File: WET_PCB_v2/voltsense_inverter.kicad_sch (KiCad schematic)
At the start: 9 parts, among them J17 Capacitor connector, J19 Capacitor connector, U3 Opamp_Quad

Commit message: notees
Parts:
- removed D7, D8: 1N4004, Diode_THT:D_DO-15_P2.54mm_Vertical_CathodeUp, symbol Diode:1N4004
- added D31, D32: D_Zener, Diode_THT:D_DO-15_P2.54mm_Vertical_CathodeUp, symbol Device:D_Zener
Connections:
- net GND: now also D32.2 (A)
- net VDD_OPAMP: now also D31.1 (K)
- net Vsense_ADC: now also D31.2 (A), D32.1 (K)
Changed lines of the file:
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@@
-	)
-	(symbol
-		(lib_id "Diode:1N4004")
-		(at 128.27 45.72 90)
-		(mirror x)
-		(unit 1)
-		(body_style 1)
-		(exclude_from_sim no)
-		(in_bom yes)
-		(on_board yes)
-		(in_pos_files yes)
-		(dnp no)
-		(fields_autoplaced yes)
-		(property "Reference" "D7"
-			(at 130.81 44.4499 90)
-			(show_name no)
-			(do_not_autoplace no)
-			(effects
-				(font
-					(size 1.27 1.27)
-				)
-				(justify right)
-			)
-		)
-		(property "Value" "1N4004"
-			(at 130.81 46.9899 90)
-			(show_name no)
-			(do_not_autoplace no)
-			(effects
-				(font
-					(size 1.27 1.27)
-				)
-				(justify right)
-			)
-		)
-		(property "Footprint" "Diode_THT:D_DO-15_P2.54mm_Vertical_CathodeUp"
-			(at 132.715 45.72 0)
-			(hide yes)
-			(show_name no)
-			(do_not_autoplace no)
-			(effects
-				(font
-					(size 1.27 1.27)
-				)
-			)
-		)
-		(property "Datasheet" "http://www.vishay.com/docs/88503/1n4001.pdf"
-			(at 128.27 45.72 0)
-			(hide yes)
-			(show_name no)
-			(do_not_autoplace no)
-			(effects
-				(font
-					(size 1.27 1.27)
-				)
-			)
-		)
-		(property "Description" "400V 1A General Purpose Rectifier Diode, DO-41"
-			(at 128.27 45.72 0)
-			(hide yes)
-			(show_name no)
-			(do_not_autoplace no)
-			(effects
-				(font
-					(size 1.27 1.27)
-				)
-			)
-		)
-		(property "Sim.Device" "D"
-			(at 128.27 45.72 0)
-			(hide yes)
-			(show_name no)
-			(do_not_autoplace no)
-			(effects
-				(font
-					(size 1.27 1.27)
-				)
-			)
-		)
-		(property "Sim.Pins" "1=K 2=A"
-			(at 128.27 45.72 0)
-			(hide yes)
-			(show_name no)
-			(do_not_autoplace no)
-			(effects
-				(font
-					(size 1.27 1.27)
-				)
-			)
-		)
-		(pin "1"
-		)
-		(pin "2"
-		)
-		(instances
-			(project "WET_PCB_v2"
-				(path "/13451c35-1666-47d9-9525-8d8125ba1cf3/419c9796-b7e1-43c1-b033-dc2479750a67"
-					(reference "D7")
-					(unit 1)
-				)
-			)
-		)
 	)
 	(symbol
@@
 	)
 	(symbol
+		(lib_id "Device:D_Zener")
+		(at 128.27 45.72 270)
+		(unit 1)
+		(body_style 1)
+		(exclude_from_sim no)
+		(in_bom yes)
+		(on_board yes)
+		(in_pos_files yes)
+		(dnp no)
+		(fields_autoplaced yes)
+		(property "Reference" "D31"
+			(at 130.81 44.4499 90)
+			(show_name no)
+			(do_not_autoplace no)
+			(effects
+				(font
+					(size 1.27 1.27)
+				)
+				(justify left)
+			)
+		)
+		(property "Value" "D_Zener"
+			(at 130.81 46.9899 90)
+			(show_name no)
+			(do_not_autoplace no)
+			(effects
+				(font
+					(size 1.27 1.27)
+				)
+				(justify left)
+			)
+		)
+		(property "Footprint" "Diode_THT:D_DO-15_P2.54mm_Vertical_CathodeUp"
+			(at 128.27 45.72 0)
+			(hide yes)
+			(show_name no)
+			(do_not_autoplace no)
+			(effects
+				(font
+					(size 1.27 1.27)
+				)
+			)
+		)
+		(property "Datasheet" ""
+			(at 128.27 45.72 0)
+			(hide yes)
+			(show_name no)
+			(do_not_autoplace no)
+			(effects
+				(font
+					(size 1.27 1.27)
+				)
+			)
+		)
+		(property "Description" "Zener diode"
+			(at 128.27 45.72 0)
+			(hide yes)
+			(show_name no)
+			(do_not_autoplace no)
+			(effects
+				(font
+					(size 1.27 1.27)
+				)
+			)
+		)
+		(pin "2"
+		)
+		(pin "1"
+		)
+		(instances
+			(project "WET_PCB_v2"
+				(path "/13451c35-1666-47d9-9525-8d8125ba1cf3/419c9796-b7e1-43c1-b033-dc2479750a67"
+					(reference "D31")
+					(unit 1)
+				)
+			)
+		)
+	)
+	(symbol
 		(lib_id "Connector_Generic:Conn_02x01")
 		(at 62.23 59.69 90)
@@
 	)
 	(symbol
+		(lib_id "Device:D_Zener")
+		(at 128.27 55.88 270)
+		(unit 1)
+		(body_style 1)
+		(exclude_from_sim no)
+		(in_bom yes)
+		(on_board yes)
+		(in_pos_files yes)
+		(dnp no)
+		(fields_autoplaced yes)
+		(property "Reference" "D32"
+			(at 130.81 54.6099 90)
+			(show_name no)
+			(do_not_autoplace no)
+			(effects
+				(font
+					(size 1.27 1.27)
+				)
+				(justify left)
+			)
+		)
+		(property "Value" "D_Zener"
+			(at 130.81 57.1499 90)
+			(show_name no)
+			(do_not_autoplace no)
+			(effects
+				(font
+					(size 1.27 1.27)
+				)
+				(justify left)
+			)
+		)
+		(property "Footprint" "Diode_THT:D_DO-15_P2.54mm_Vertical_CathodeUp"
+			(at 128.27 55.88 0)
+			(hide yes)
+			(show_name no)
+			(do_not_autoplace no)
+			(effects
+				(font
+					(size 1.27 1.27)
+				)
+			)
+		)
+		(property "Datasheet" ""
+			(at 128.27 55.88 0)
+			(hide yes)
+			(show_name no)
+			(do_not_autoplace no)
+			(effects
+				(font
+					(size 1.27 1.27)
+				)
+			)
+		)
+		(property "Description" "Zener diode"
+			(at 128.27 55.88 0)
+			(hide yes)
+			(show_name no)
+			(do_not_autoplace no)
+			(effects
+				(font
+					(size 1.27 1.27)
+				)
+			)
+		)
+		(pin "2"
+		)
+		(pin "1"
+		)
+		(instances
+			(project "WET_PCB_v2"
+				(path "/13451c35-1666-47d9-9525-8d8125ba1cf3/419c9796-b7e1-43c1-b033-dc2479750a67"
+					(reference "D32")
+					(unit 1)
+				)
+			)
+		)
+	)
+	(symbol
 		(lib_id "power:GND")
 		(at 128.27 59.69 0)
@@
 					(unit 1)
 				)
-			)
-		)
-	)
-	(symbol
-		(lib_id "Diode:1N4004")
-		(at 128.27 55.88 90)
-		(mirror x)
-		(unit 1)
-		(body_style 1)
-		(exclude_from_sim no)
-		(in_bom yes)
-		(on_board yes)
-		(in_pos_files yes)
-		(dnp no)
-		(fields_autoplaced yes)
-		(property "Reference" "D8"
-			(at 130.81 54.6099 90)
-			(show_name no)
-			(do_not_autoplace no)
-			(effects
-				(font
-					(size 1.27 1.27)
-				)
-				(justify right)
-			)
-		)
-		(property "Value" "1N4004"
-			(at 130.81 57.1499 90)
-			(show_name no)
-			(do_not_autoplace no)
-			(effects
-				(font
-					(size 1.27 1.27)
-				)
-				(justify right)
-			)
-		)
-		(property "Footprint" "Diode_THT:D_DO-15_P2.54mm_Vertical_CathodeUp"
-			(at 132.715 55.88 0)
-			(hide yes)
-			(show_name no)
-			(do_not_autoplace no)
-			(effects
-				(font
-					(size 1.27 1.27)
-				)
-			)
-		)
-		(property "Datasheet" "http://www.vishay.com/docs/88503/1n4001.pdf"
-			(at 128.27 55.88 0)
-			(hide yes)
-			(show_name no)
-			(do_not_autoplace no)
-			(effects
-				(font
-					(size 1.27 1.27)
-				)
-			)
-		)
-		(property "Description" "400V 1A General Purpose Rectifier Diode, DO-41"
-			(at 128.27 55.88 0)
-			(hide yes)
-			(show_name no)
-			(do_not_autoplace no)
-			(effects
-				(font
-					(size 1.27 1.27)
-				)
-			)
-		)
-		(property "Sim.Device" "D"
-			(at 128.27 55.88 0)
-			(hide yes)
-			(show_name no)
-			(do_not_autoplace no)
-			(effects
-				(font
-					(size 1.27 1.27)
-				)
-			)
-		)
-		(property "Sim.Pins" "1=K 2=A"
-			(at 128.27 55.88 0)
-			(hide yes)
-			(show_name no)
-			(do_not_autoplace no)
-			(effects
-				(font
-					(size 1.27 1.27)
-				)
-			)
-		)
-		(pin "1"
-		)
-		(pin "2"
-		)
-		(instances
-			(project "WET_PCB_v2"
-				(path "/13451c35-1666-47d9-9525-8d8125ba1cf3/419c9796-b7e1-43c1-b033-dc2479750a67"
-					(reference "D8")
-					(unit 1)
-				)

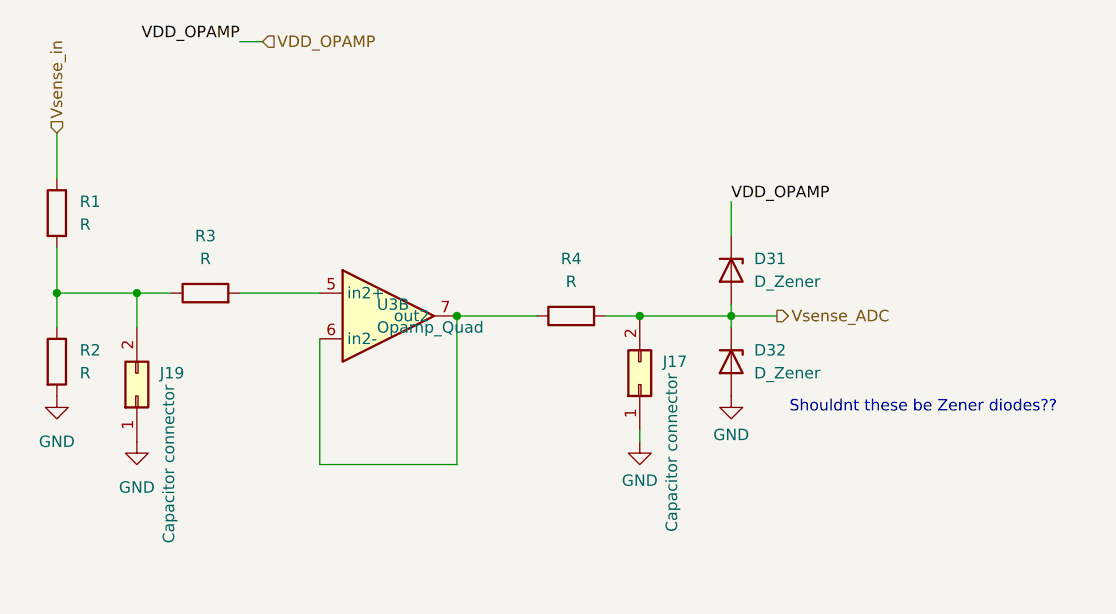
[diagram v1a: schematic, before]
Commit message: redid part of layout inverter
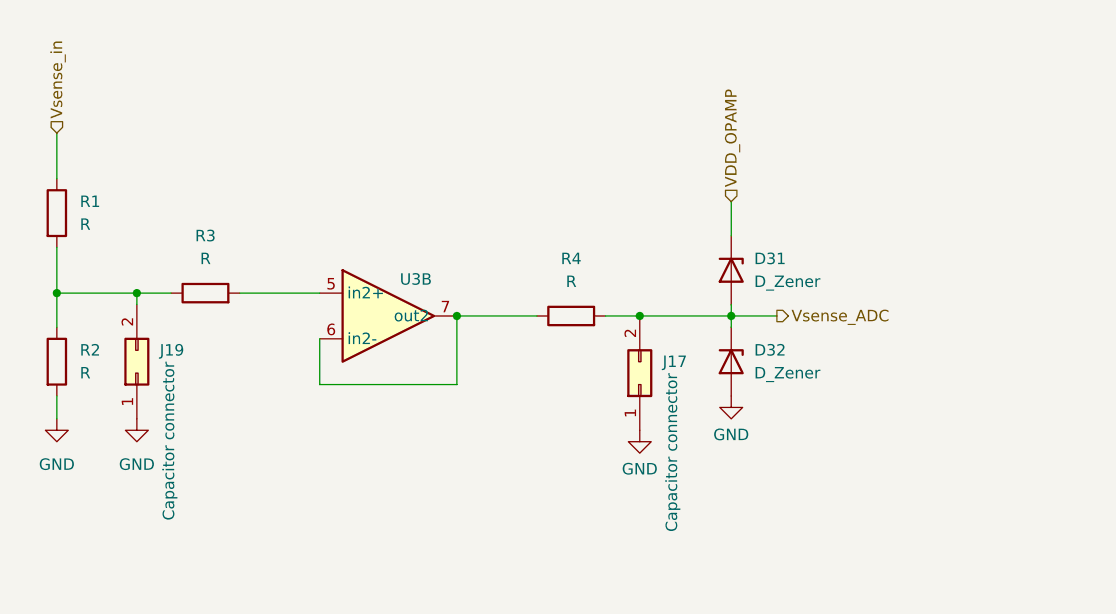
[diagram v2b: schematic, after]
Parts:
- R1, R2, R3, R4: footprint Resistor_THT:R_Axial_DIN0207_L6.3mm_D2.5mm_P7.62mm_Horizontal -> Resistor_SMD:R_0805_2012Metric_Pad1.20x1.40mm_HandSolder
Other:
- note removed: "Shouldnt these be Zener diodes??"
- moved on the sheet: J19
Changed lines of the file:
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@@
 	(generator_version "10.0")
 	(paper "A4")
-	(text "Shouldnt these be Zener diodes??\n"
-		(exclude_from_sim no)
-		(at 149.606 60.96 0)
-		(effects
-			(font
-				(size 1.27 1.27)
-			)
-		)
-	)
 	(junction
 		(at 53.34 48.26)
@@
 	)
 	(junction
+		(at 62.23 48.26)
+		(diameter 0)
+		(color 0 0 0 0)
+	)
+	(junction
 		(at 128.27 50.8)
 		(diameter 0)
@@
 	)
 	(junction
-		(at 62.23 48.26)
+		(at 118.11 50.8)
 		(diameter 0)
 		(color 0 0 0 0)
@@
 		(color 0 0 0 0)
 	)
-	(junction
-		(at 118.11 50.8)
-		(diameter 0)
-		(color 0 0 0 0)
-	)
-	(wire
-		(pts
-			(xy 62.23 48.26) (xy 62.23 52.07)
-		)
-		(stroke
-			(width 0)
-			(type default)
-		)
-	)
 	(wire
 		(pts
@@
 	(wire
 		(pts
-			(xy 82.55 53.34) (xy 82.55 67.31)
+			(xy 82.55 53.34) (xy 82.55 58.42)
 		)
 		(stroke
@@
 	(wire
 		(pts
+			(xy 62.23 49.53) (xy 62.23 48.26)
+		)
+		(stroke
+			(width 0)
+			(type default)
+		)
+	)
+	(wire
+		(pts
 			(xy 114.3 50.8) (xy 118.11 50.8)
 		)
@@
 	(wire
 		(pts
-			(xy 118.11 63.5) (xy 118.11 64.77)
-		)
-		(stroke
-			(width 0)
-			(type default)
-		)
-	)
-	(wire
-		(pts
 			(xy 53.34 48.26) (xy 53.34 52.07)
 		)
@@
 	(wire
 		(pts
-			(xy 97.79 50.8) (xy 97.79 67.31)
+			(xy 97.79 50.8) (xy 97.79 58.42)
+		)
+		(stroke
+			(width 0)
+			(type default)
+		)
+	)
+	(wire
+		(pts
+			(xy 53.34 62.23) (xy 53.34 59.69)
 		)
 		(stroke
@@
 	(wire
 		(pts
-			(xy 76.2 20.32) (xy 73.66 20.32)
-		)
-		(stroke
-			(width 0)
-			(type default)
-		)
-	)
-	(wire
-		(pts
 			(xy 62.23 48.26) (xy 66.04 48.26)
 		)
@@
 	(wire
 		(pts
-			(xy 82.55 67.31) (xy 97.79 67.31)
-		)
-		(stroke
-			(width 0)
-			(type default)
-		)
-	)
-	(label "VDD_OPAMP"
-		(at 128.27 38.1 0)
-		(effects
-			(font
-				(size 1.27 1.27)
-			)
-			(justify left bottom)
-		)
-	)
-	(label "VDD_OPAMP"
-		(at 73.66 20.32 180)
-		(effects
-			(font
-				(size 1.27 1.27)
-			)
-			(justify right bottom)
-		)
-	)
-	(hierarchical_label "VDD_OPAMP"
-		(shape input)
-		(at 76.2 20.32 0)
-		(effects
-			(font
-				(size 1.27 1.27)
-			)
-			(justify left)
+			(xy 82.55 58.42) (xy 97.79 58.42)
+		)
+		(stroke
+			(width 0)
+			(type default)
 		)
 	)
@@
 		(shape input)
 		(at 53.34 30.48 90)
+		(effects
+			(font
+				(size 1.27 1.27)
+			)
+			(justify left)
+		)
+	)
+	(hierarchical_label "VDD_OPAMP"
+		(shape input)
+		(at 128.27 38.1 90)
 		(effects
 			(font
@@
 			)
 		)
-		(property "Footprint" "Resistor_THT:R_Axial_DIN0207_L6.3mm_D2.5mm_P7.62mm_Horizontal"
+		(property "Footprint" "Resistor_SMD:R_0805_2012Metric_Pad1.20x1.40mm_HandSolder"
 			(at 110.49 52.578 90)
 			(hide yes)
@@
 			)
 		)
-		(property "Footprint" "Resistor_THT:R_Axial_DIN0207_L6.3mm_D2.5mm_P7.62mm_Horizontal"
+		(property "Footprint" "Resistor_SMD:R_0805_2012Metric_Pad1.20x1.40mm_HandSolder"
 			(at 51.562 55.88 90)
 			(hide yes)
@@
 	(symbol
 		(lib_id "Connector_Generic:Conn_02x01")
-		(at 62.23 59.69 90)
+		(at 62.23 57.15 90)
 		(unit 1)
 		(body_style 1)
@@
 		(dnp no)
 		(property "Reference" "J19"
-			(at 64.77 57.1499 90)
+			(at 64.77 54.6099 90)
 			(show_name no)
 			(do_not_autoplace no)
@@
 		)
 		(property "Value" "Capacitor connector"
-			(at 65.786 58.42 0)
+			(at 65.786 55.88 0)
 			(show_name no)
 			(do_not_autoplace no)
@@
 		)
 		(property "Footprint" "Connector_PinSocket_2.54mm:PinSocket_1x02_P2.54mm_Vertical"
-			(at 62.23 59.69 0)
+			(at 62.23 57.15 0)
 			(hide yes)
 			(show_name no)
@@
 		)
 		(property "Datasheet" ""
-			(at 62.23 59.69 0)
+			(at 62.23 57.15 0)
 			(hide yes)
 			(show_name no)
@@
 		)
 		(property "Description" "Generic connector, double row, 02x01, this symbol is compatible with counter-clockwise, top-bottom and odd-even numbering schemes., script generated (kicad-library-utils/schlib/autogen/connector/)"
-			(at 62.23 59.69 0)
+			(at 62.23 57.15 0)
 			(hide yes)
 			(show_name no)
@@
 	(symbol
 		(lib_id "power:GND")
-		(at 62.23 64.77 0)
+		(at 62.23 62.23 0)
 		(unit 1)
 		(body_style 1)
@@
 		(fields_autoplaced yes)
 		(property "Reference" "#PWR018"
-			(at 62.23 71.12 0)
+			(at 62.23 68.58 0)
 			(hide yes)
 			(show_name no)
@@
 		)
 		(property "Value" "GND"
-			(at 62.23 69.85 0)
+			(at 62.23 67.31 0)
 			(show_name no)
 			(do_not_autoplace no)
@@
 		)
 		(property "Footprint" ""
-			(at 62.23 64.77 0)
+			(at 62.23 62.23 0)
 			(hide yes)
 			(show_name no)
@@
 		)
 		(property "Datasheet" ""
-			(at 62.23 64.77 0)
+			(at 62.23 62.23 0)
 			(hide yes)
 			(show_name no)
@@
 		)
 		(property "Description" "Power symbol creates a global label with name \"GND\" , ground"
-			(at 62.23 64.77 0)
+			(at 62.23 62.23 0)
 			(hide yes)
 			(show_name no)
@@
 			)
 		)
-		(property "Footprint" "Resistor_THT:R_Axial_DIN0207_L6.3mm_D2.5mm_P7.62mm_Horizontal"
+		(property "Footprint" "Resistor_SMD:R_0805_2012Metric_Pad1.20x1.40mm_HandSolder"
 			(at 69.85 50.038 90)
 			(hide yes)
@@
 		(in_pos_files yes)
 		(dnp no)
-		(fields_autoplaced yes)
 		(property "Reference" "U3"
-			(at 88.9 49.5299 0)
+			(at 91.44 46.736 0)
 			(show_name no)
 			(do_not_autoplace no)
@@
 		)
 		(property "Value" "Opamp_Quad"
-			(at 88.9 52.0699 0)
+			(at 84.836 57.15 0)
+			(hide yes)
 			(show_name no)
 			(do_not_autoplace no)
@@
 	(symbol
 		(lib_id "power:GND")
-		(at 118.11 64.77 0)
+		(at 118.11 63.5 0)
 		(unit 1)
 		(body_style 1)
@@
 		(dnp no)
 		(property "Reference" "#PWR021"
-			(at 118.11 71.12 0)
+			(at 118.11 69.85 0)
 			(hide yes)
 			(show_name no)
@@
 		)
 		(property "Value" "GND"
-			(at 118.11 69.088 0)
+			(at 118.11 67.818 0)
 			(show_name no)
 			(do_not_autoplace no)
@@
 		)
 		(property "Footprint" ""
-			(at 118.11 64.77 0)
+			(at 118.11 63.5 0)
 			(hide yes)
 			(show_name no)
@@
 		)
 		(property "Datasheet" ""
-			(at 118.11 64.77 0)
+			(at 118.11 63.5 0)
 			(hide yes)
 			(show_name no)
@@
 		)
 		(property "Description" "Power symbol creates a global label with name \"GND\" , ground"
-			(at 118.11 64.77 0)
+			(at 118.11 63.5 0)
 			(hide yes)
 			(show_name no)
@@
 			)
 		)
-		(property "Footprint" "Resistor_THT:R_Axial_DIN0207_L6.3mm_D2.5mm_P7.62mm_Horizontal"
+		(property "Footprint" "Resistor_SMD:R_0805_2012Metric_Pad1.20x1.40mm_HandSolder"
 			(at 51.562 39.37 90)
 			(hide yes)
@@
 	(symbol
 		(lib_id "power:GND")
-		(at 53.34 59.69 0)
+		(at 53.34 62.23 0)
 		(unit 1)
 		(body_style 1)
@@
 		(fields_autoplaced yes)
 		(property "Reference" "#PWR017"
-			(at 53.34 66.04 0)
+			(at 53.34 68.58 0)
 			(hide yes)
 			(show_name no)
@@
 		)
 		(property "Value" "GND"
-			(at 53.34 64.77 0)
+			(at 53.34 67.31 0)
 			(show_name no)
 			(do_not_autoplace no)
@@
 		)
 		(property "Footprint" ""
-			(at 53.34 59.69 0)
+			(at 53.34 62.23 0)
 			(hide yes)
 			(show_name no)
@@
 		)
 		(property "Datasheet" ""
-			(at 53.34 59.69 0)
+			(at 53.34 62.23 0)
 			(hide yes)
 			(show_name no)
@@
 		)
 		(property "Description" "Power symbol creates a global label with name \"GND\" , ground"
-			(at 53.34 59.69 0)
-			(hide yes)
-			(show_name no)
+			(at 53.34 62.23 0)
+			(hide yes)
+			(show_name no)

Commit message: didnt watch the lecture but made progress ig
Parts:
- added R41: R0, Resistor_SMD:R_0805_2012Metric_Pad1.20x1.40mm_HandSolder, symbol Device:R
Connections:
- net at R4.1, U3.7 (out2): now also R41.2; no longer U3.6 (in2-)
- new net: R41.1, U3.6 (in2-)
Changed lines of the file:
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@@
+	)
+	(junction
+		(at 100.33 50.8)
+		(diameter 0)
+		(color 0 0 0 0)
 	)
 	(junction
@@
 		(color 0 0 0 0)
 	)
-	(junction
-		(at 97.79 50.8)
-		(diameter 0)
-		(color 0 0 0 0)
+	(wire
+		(pts
+			(xy 95.25 58.42) (xy 100.33 58.42)
+		)
+		(stroke
+			(width 0)
+			(type default)
+		)
 	)
 	(wire
@@
 	(wire
 		(pts
-			(xy 97.79 50.8) (xy 106.68 50.8)
+			(xy 97.79 50.8) (xy 100.33 50.8)
 		)
 		(stroke
@@
 	(wire
 		(pts
+			(xy 100.33 50.8) (xy 106.68 50.8)
+		)
+		(stroke
+			(width 0)
+			(type default)
+		)
+	)
+	(wire
+		(pts
 			(xy 53.34 48.26) (xy 53.34 52.07)
 		)
@@
 	(wire
 		(pts
+			(xy 82.55 58.42) (xy 87.63 58.42)
+		)
+		(stroke
+			(width 0)
+			(type default)
+		)
+	)
+	(wire
+		(pts
 			(xy 128.27 38.1) (xy 128.27 41.91)
 		)
@@
 	(wire
 		(pts
-			(xy 97.79 50.8) (xy 97.79 58.42)
+			(xy 100.33 50.8) (xy 100.33 58.42)
 		)
 		(stroke
@@
 		(pts
 			(xy 62.23 48.26) (xy 66.04 48.26)
-		)
-		(stroke
-			(width 0)
-			(type default)
-		)
-	)
-	(wire
-		(pts
-			(xy 82.55 58.42) (xy 97.79 58.42)
 		)
 		(stroke
@@
 					(unit 1)
 				)
+			)
+		)
+	)
+	(symbol
+		(lib_id "Device:R")
+		(at 91.44 58.42 90)
+		(unit 1)
+		(body_style 1)
+		(exclude_from_sim no)
+		(in_bom yes)
+		(on_board yes)
+		(in_pos_files yes)
+		(dnp no)
+		(fields_autoplaced yes)
+		(property "Reference" "R41"
+			(at 91.44 52.07 90)
+			(show_name no)
+			(do_not_autoplace no)
+			(effects
+				(font
+					(size 1.27 1.27)
+				)
+			)
+		)
+		(property "Value" "R0"
+			(at 91.44 54.61 90)
+			(show_name no)
+			(do_not_autoplace no)
+			(effects
+				(font
+					(size 1.27 1.27)
+				)
+			)
+		)
+		(property "Footprint" "Resistor_SMD:R_0805_2012Metric_Pad1.20x1.40mm_HandSolder"
+			(at 91.44 60.198 90)
+			(hide yes)
+			(show_name no)
+			(do_not_autoplace no)
+			(effects
+				(font
+					(size 1.27 1.27)
+				)
+			)
+		)
+		(property "Datasheet" ""
+			(at 91.44 58.42 0)
+			(hide yes)
+			(show_name no)
+			(do_not_autoplace no)
+			(effects
+				(font
+					(size 1.27 1.27)
+				)
+			)
+		)
+		(property "Description" "Resistor"
+			(at 91.44 58.42 0)
+			(hide yes)
+			(show_name no)
+			(do_not_autoplace no)
+			(effects
+				(font
+					(size 1.27 1.27)
+				)
+			)
+		)
+		(pin "2"
+		)
+		(pin "1"
+		)
+		(instances
+			(project "WET_PCB_v2"
+				(path "/13451c35-1666-47d9-9525-8d8125ba1cf3/419c9796-b7e1-43c1-b033-dc2479750a67"
+					(reference "R41")
+					(unit 1)
+				)
